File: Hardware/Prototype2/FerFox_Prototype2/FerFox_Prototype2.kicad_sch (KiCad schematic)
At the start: 12 parts, among them J1 Conn_01x08_Pin, J2 SD_Card, U1 STM32F767ZITx, U2 LY68L6400, Y1 8MHz

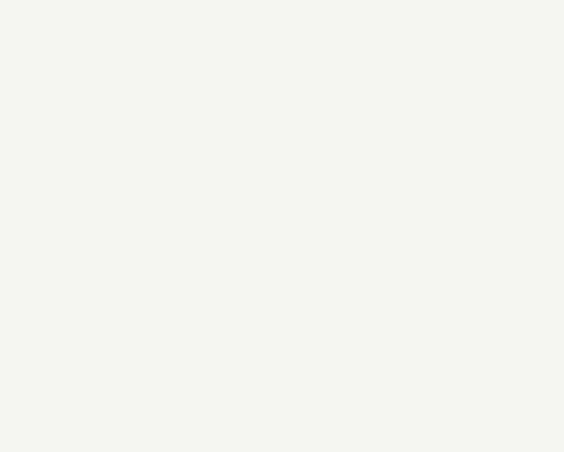
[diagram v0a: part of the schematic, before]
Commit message: Second prototype with STM32F767ZIT6U, just created a project.
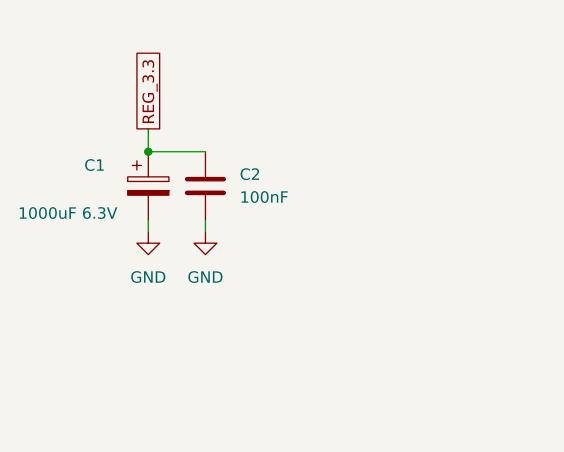
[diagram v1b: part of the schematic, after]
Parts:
- added C1: 1000uF 6.3V, symbol Device:C_Polarized
- added C2: 100nF, symbol Device:C
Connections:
- net GND: now also C1.2, C2.1
- net REG_3.3: now also C1.1, C2.2

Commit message: Initial QSPI RAM operations
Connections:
- net PSRAM_#CS: now also U1.136 (PB6); no longer U1.15 (PF5)
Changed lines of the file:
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@@
-	(wire
-		(pts
-			(xy 152.4 161.29) (xy 154.94 161.29)
-		)
-		(stroke
-			(width 0)
-			(type default)
-		)
-	)
 	(wire
 		(pts
@@
 		(pts
 			(xy 215.9 92.71) (xy 218.44 92.71)
+		)
+		(stroke
+			(width 0)
+			(type default)
+		)
+	)
+	(wire
+		(pts
+			(xy 215.9 138.43) (xy 218.44 138.43)
 		)
 		(stroke
@@
 		)
 	)
-	(global_label "PSRAM_#CS"
-		(shape output)
-		(at 152.4 161.29 180)
-		(fields_autoplaced yes)
-		(effects
-			(font
-				(size 1.27 1.27)
-			)
-			(justify right)
-		)
-		(property "Intersheetrefs" "${INTERSHEET_REFS}"
-			(at 138.4082 161.29 0)
-			(effects
-				(font
-					(size 1.27 1.27)
-				)
-				(justify right)
-				(hide yes)
-			)
-		)
-	)
 	(global_label "DISP_#RST"
 		(shape input)
@@
 			(effects
 				(font
+					(size 1.27 1.27)
+				)
+				(justify left)
+				(hide yes)
+			)
+		)
+	)
+	(global_label "PSRAM_#CS"
+		(shape output)
+		(at 218.44 138.43 0)
+		(fields_autoplaced yes)
+		(effects
+			(font
+				(size 1.27 1.27)
+			)
+			(justify left)
+		)
+		(property "Intersheetrefs" "${INTERSHEET_REFS}"
+			(at 232.4318 138.43 0)
+			(effects
+				(font

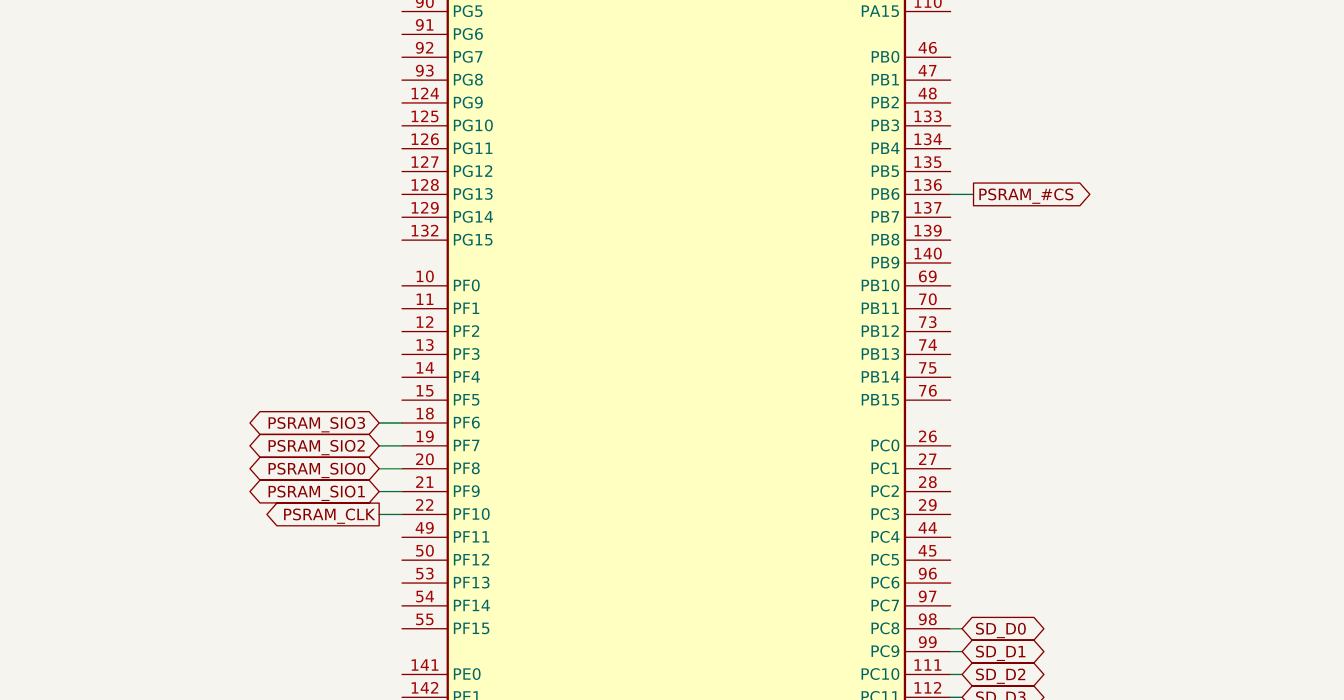
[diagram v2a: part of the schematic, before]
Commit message: PSRAM QSPI read/write OK, time for DMA
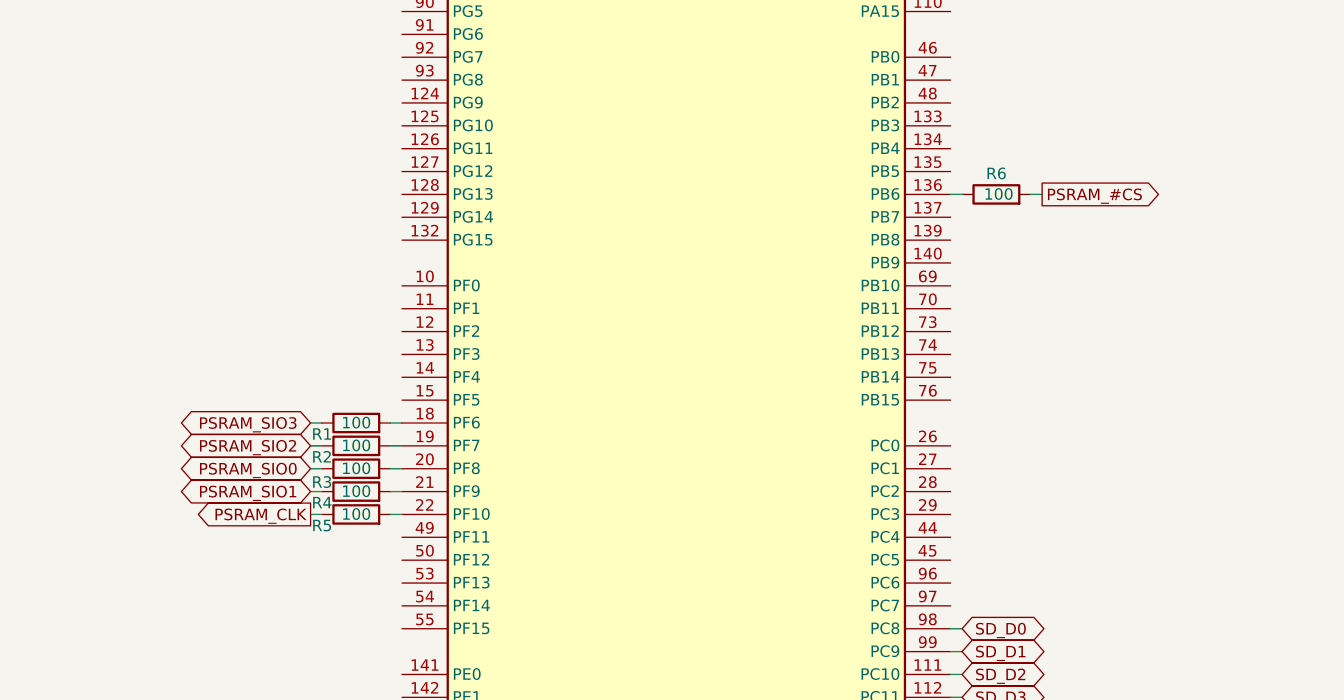
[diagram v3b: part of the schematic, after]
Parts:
- added R1, R2, R3, R4, R5, R6: 100, symbol Device:R
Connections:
- net PSRAM_#CS: now also R6.2; no longer U1.136 (PB6)
- net PSRAM_CLK: now also R5.1; no longer U1.22 (PF10)
- net PSRAM_SIO0: now also R3.1; no longer U1.20 (PF8)
- net PSRAM_SIO1: now also R4.1; no longer U1.21 (PF9)
- net PSRAM_SIO2: now also R2.1; no longer U1.19 (PF7)
- net PSRAM_SIO3: now also R1.1; no longer U1.18 (PF6)
- new net: R1.2, U1.18 (PF6)
- new net: R2.2, U1.19 (PF7)
- new net: R6.1, U1.136 (PB6)
- new net: R5.2, U1.22 (PF10)
- new net: R3.2, U1.20 (PF8)
- new net: R4.2, U1.21 (PF9)

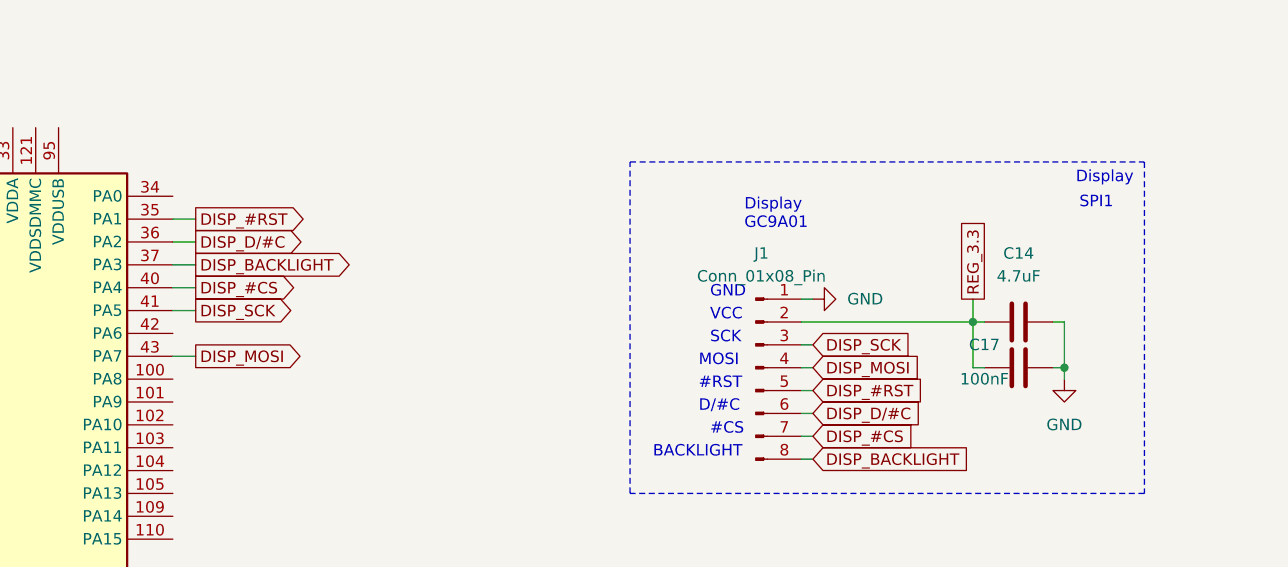
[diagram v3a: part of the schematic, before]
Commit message: Display is working with old driver
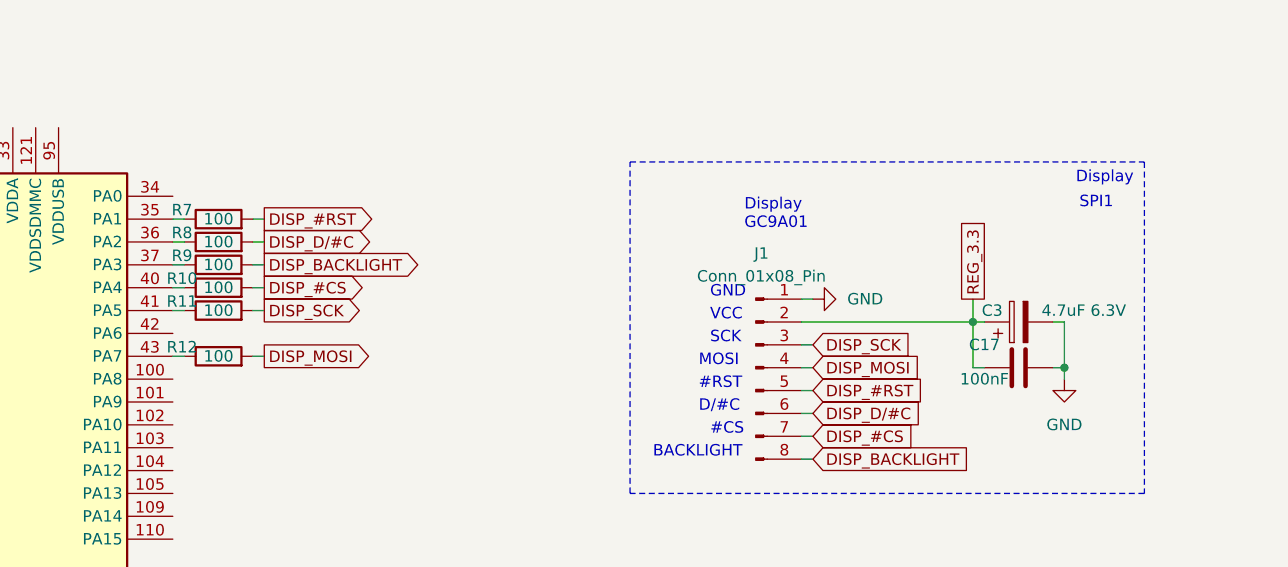
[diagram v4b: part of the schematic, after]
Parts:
- removed C14: 4.7uF, symbol Device:C
- added C3: 4.7uF 6.3V, symbol Device:C_Polarized
- added R10, R11, R12, R7, R8, R9: 100, symbol Device:R
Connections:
- net DISP_#CS: now also R10.2; no longer U1.40 (PA4)
- net DISP_#RST: now also R7.2; no longer U1.35 (PA1)
- net DISP_BACKLIGHT: now also R9.2; no longer U1.37 (PA3)
- net DISP_D/#C: now also R8.2; no longer U1.36 (PA2)
- net DISP_MOSI: now also R12.2; no longer U1.43 (PA7)
- net DISP_SCK: now also R11.2; no longer U1.41 (PA5)
- net GND: now also C3.2
- net REG_3.3: now also C3.1
- new net: R9.1, U1.37 (PA3)
- new net: R7.1, U1.35 (PA1)
- new net: R10.1, U1.40 (PA4)
- new net: R8.1, U1.36 (PA2)
- new net: R11.1, U1.41 (PA5)
- new net: R12.1, U1.43 (PA7)

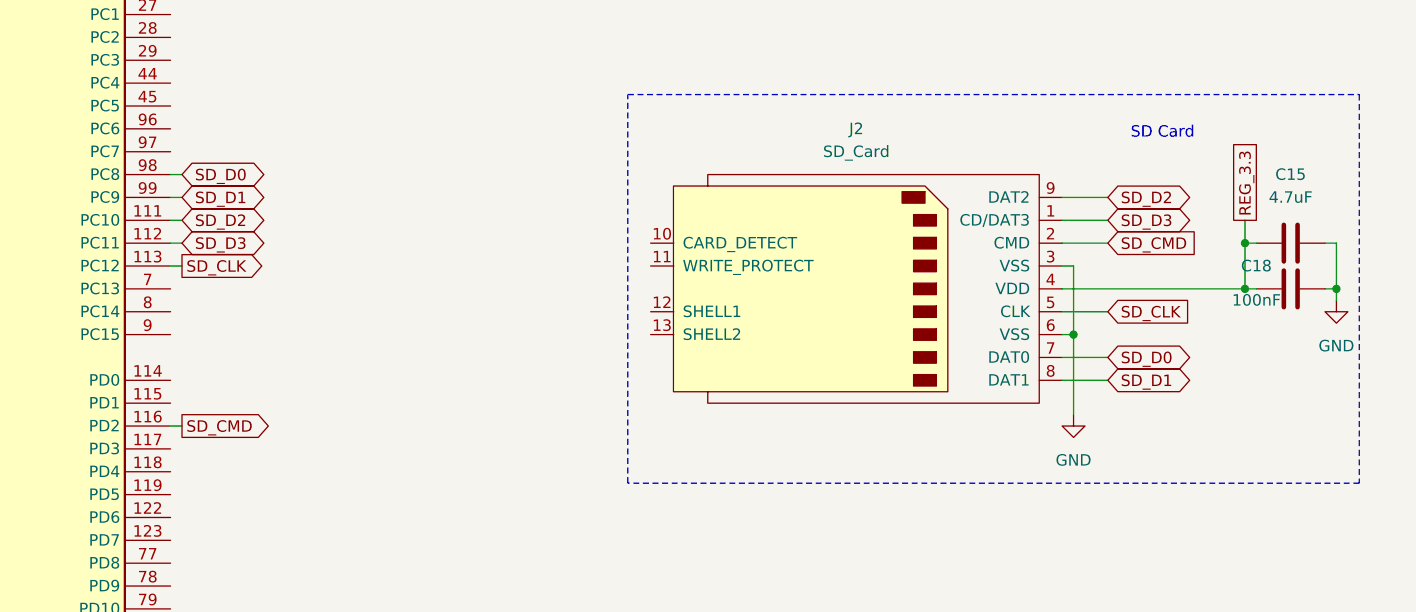
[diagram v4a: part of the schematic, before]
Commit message: SDCARD read PIO mode
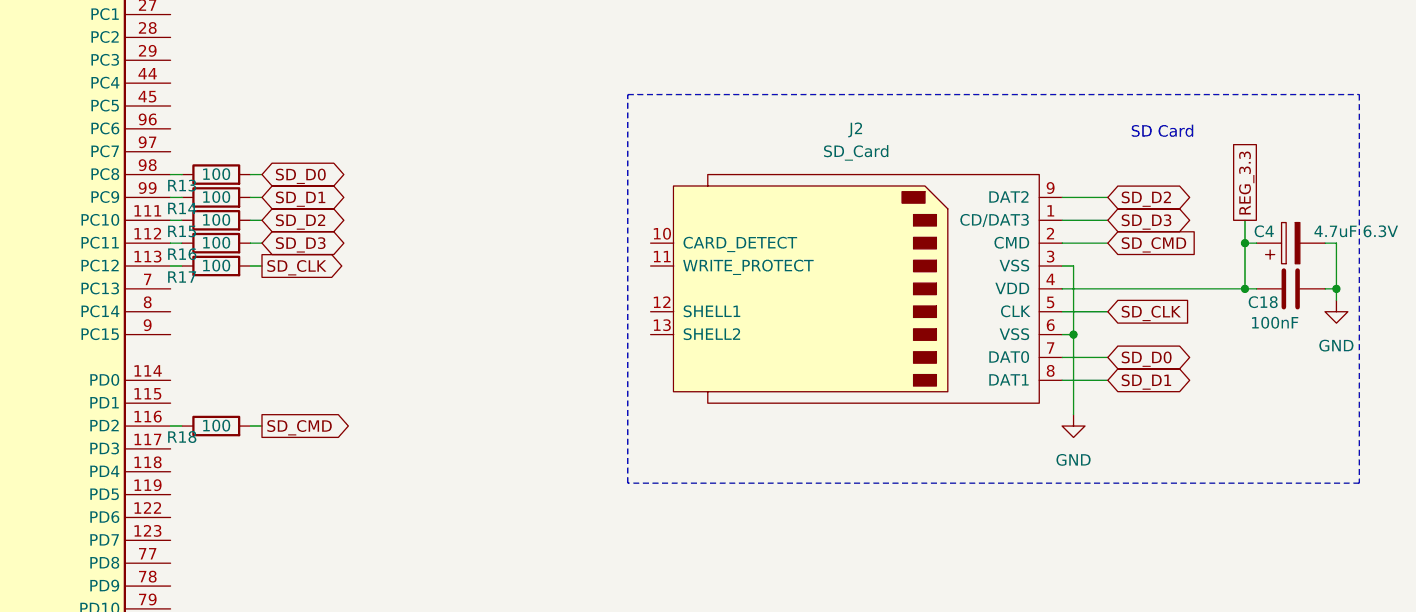
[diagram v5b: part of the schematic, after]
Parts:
- removed C15: 4.7uF, symbol Device:C
- added C4: 4.7uF 6.3V, symbol Device:C_Polarized
- added R13, R14, R15, R16, R17, R18: 100, symbol Device:R
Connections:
- net GND: now also C4.2
- net REG_3.3: now also C4.1
- net SD_CLK: now also R17.2; no longer U1.113 (PC12)
- net SD_CMD: now also R18.2; no longer U1.116 (PD2)
- net SD_D0: now also R13.2; no longer U1.98 (PC8)
- net SD_D1: now also R14.2; no longer U1.99 (PC9)
- net SD_D2: now also R15.2; no longer U1.111 (PC10)
- net SD_D3: now also R16.2; no longer U1.112 (PC11)
- new net: R18.1, U1.116 (PD2)
- new net: R17.1, U1.113 (PC12)
- new net: R13.1, U1.98 (PC8)
- new net: R16.1, U1.112 (PC11)
- new net: R15.1, U1.111 (PC10)
- new net: R14.1, U1.99 (PC9)

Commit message: Hardware is OK, able to see animation
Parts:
- added C5: 1000uF 6.3V, symbol Device:C_Polarized
- R13, R14, R15, R16, R17, R18: value 100 -> 270
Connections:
- net GND: now also C5.2
- net REG_3.3: now also C5.1
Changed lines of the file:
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@@
 	)
 	(junction
+		(at 57.15 152.4)
+		(diameter 0)
+		(color 0 0 0 0)
+	)
+	(junction
 		(at 134.62 95.25)
 		(diameter 0)
@@
 	)
 	(junction
+		(at 67.31 152.4)
+		(diameter 0)
+		(color 0 0 0 0)
+	)
+	(junction
 		(at 144.78 102.87)
 		(diameter 0)
@@
 	(wire
 		(pts
+			(xy 67.31 146.05) (xy 67.31 152.4)
+		)
+		(stroke
+			(width 0)
+			(type default)
+		)
+	)
+	(wire
+		(pts
 			(xy 153.67 166.37) (xy 154.94 166.37)
 		)
@@
 	(wire
 		(pts
+			(xy 57.15 152.4) (xy 58.42 152.4)
+		)
+		(stroke
+			(width 0)
+			(type default)
+		)
+	)
+	(wire
+		(pts
 			(xy 215.9 186.69) (xy 217.17 186.69)
 		)
@@
 	(wire
 		(pts
+			(xy 58.42 146.05) (xy 57.15 146.05)
+		)
+		(stroke
+			(width 0)
+			(type default)
+		)
+	)
+	(wire
+		(pts
 			(xy 151.13 95.25) (xy 144.78 95.25)
 		)
@@
 	(wire
 		(pts
+			(xy 57.15 146.05) (xy 57.15 152.4)
+		)
+		(stroke
+			(width 0)
+			(type default)
+		)
+	)
+	(wire
+		(pts
 			(xy 144.78 168.91) (xy 146.05 168.91)
 		)
@@
 	(wire
 		(pts
+			(xy 66.04 146.05) (xy 67.31 146.05)
+		)
+		(stroke
+			(width 0)
+			(type default)
+		)
+	)
+	(wire
+		(pts
 			(xy 151.13 102.87) (xy 144.78 102.87)
 		)
@@
 	(wire
 		(pts
-			(xy 52.07 152.4) (xy 58.42 152.4)
+			(xy 52.07 152.4) (xy 57.15 152.4)
 		)
 		(stroke
@@
 			)
 		)
-		(property "Value" "100"
+		(property "Value" "270"
 			(at 220.98 214.63 90)
 			(effects
@@
 			)
 		)
-		(property "Value" "100"
+		(property "Value" "270"
 			(at 220.98 196.85 90)
 			(effects
@@
 			)
 		)
-		(property "Value" "100"
+		(property "Value" "270"
 			(at 220.98 186.69 90)
 			(effects
@@
 			)
 		)
-		(property "Value" "100"
+		(property "Value" "270"
 			(at 220.98 194.31 90)
 			(effects
@@
 		(on_board yes)
 		(dnp no)
-		(fields_autoplaced yes)
 		(property "Reference" "C16"
-			(at 62.23 144.78 90)
+			(at 58.928 150.622 90)
 			(effects
 				(font
@@
 		)
 		(property "Value" "100nF"
-			(at 62.23 147.32 90)
+			(at 66.548 150.368 90)
 			(effects
 				(font
@@
 	)
 	(symbol
+		(lib_id "Device:C_Polarized")
+		(at 62.23 146.05 90)
+		(unit 1)
+		(exclude_from_sim no)
+		(in_bom yes)
+		(on_board yes)
+		(dnp no)
+		(property "Reference" "C5"
+			(at 60.706 144.272 90)
+			(effects
+				(font
+					(size 1.27 1.27)
+				)
+				(justify left)
+			)
+		)
+		(property "Value" "1000uF 6.3V"
+			(at 76.2 144.272 90)
+			(effects
+				(font
+					(size 1.27 1.27)
+				)
+				(justify left)
+			)
+		)
+		(property "Footprint" ""
+			(at 66.04 145.0848 0)
+			(effects
+				(font
+					(size 1.27 1.27)
+				)
+				(hide yes)
+			)
+		)
+		(property "Datasheet" "~"
+			(at 62.23 146.05 0)
+			(effects
+				(font
+					(size 1.27 1.27)
+				)
+				(hide yes)
+			)
+		)
+		(property "Description" "Polarized capacitor"
+			(at 62.23 146.05 0)
+			(effects
+				(font
+					(size 1.27 1.27)
+				)
+				(hide yes)
+			)
+		)
+		(pin "1"
+		)
+		(pin "2"
+		)
+		(instances
+			(project "FerFox_Prototype2"
+				(path "/011f2c64-cf22-44cd-a30f-ff566a75b03a"
+					(reference "C5")
+					(unit 1)
+				)
+			)
+		)
+	)
+	(symbol
 		(lib_id "Device:R")
 		(at 220.98 97.79 90)
@@
 			)
 		)
-		(property "Value" "100"
+		(property "Value" "270"
 			(at 220.98 189.23 90)
 			(effects
@@
 			)
 		)
-		(property "Value" "100"
+		(property "Value" "270"
 			(at 220.98 191.77 90)
 			(effects
